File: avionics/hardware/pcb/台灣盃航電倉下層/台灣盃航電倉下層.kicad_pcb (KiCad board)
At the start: 4 copper layers, 80 x 80 mm, 43 parts, among them J1 XT60, J2 XT60, J4 Pyro1, J5 Pyro2, Q1 NMOS, Q2 NMOS, U3 LM2596S-5, U4 LM2596S-5, U5 AMS1117-3.3, U6 AMS1117-3.3

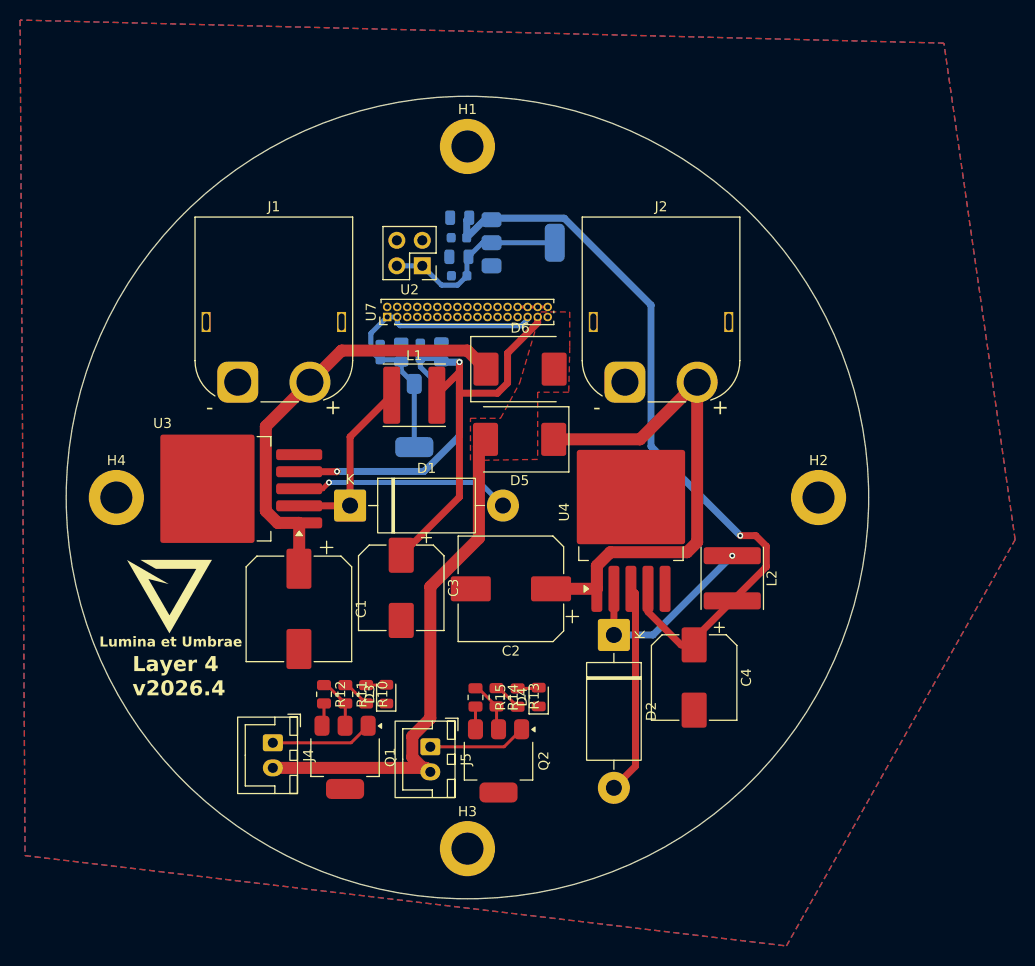
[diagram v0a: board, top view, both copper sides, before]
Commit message: Add files via upload
This is V1.1
add via stitch to increase heat dissipation capacity
change layer from 4 to 2, and increase thickness to 0.07mm
resolve the DRC problem
change the pad connection of the connector
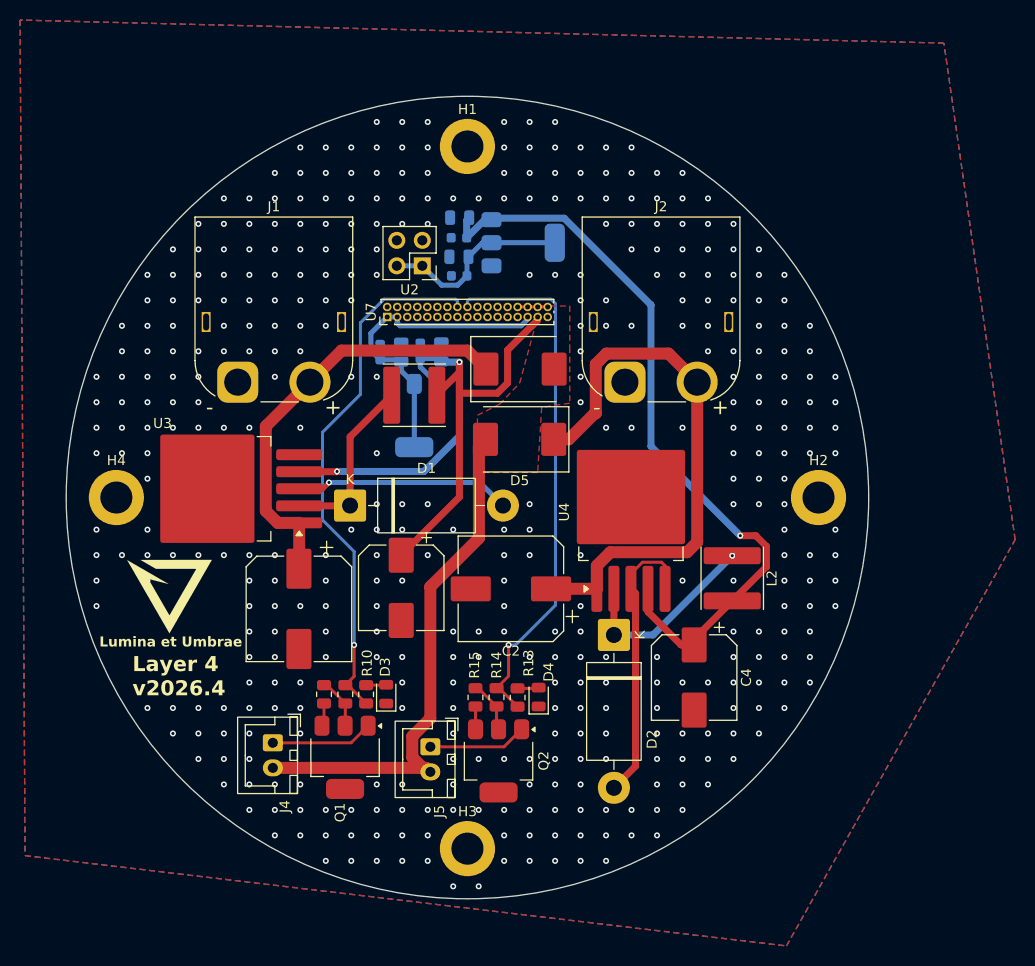
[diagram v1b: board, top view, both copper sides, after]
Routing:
- net PYRO2: track 2.87 -> 53.7 mm, vias 0 -> 1
- net PYRO1: track 2.83 -> 53.5 mm, vias 0 -> 1
- net GND: track 50.0 -> 57.8 mm, vias 1 -> 407
- net +BATT_b: track 50.4 -> 55.7 mm
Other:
- copper layers 4 -> 2

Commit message: V1.2
change Schottky Diode to nmos
change the footprint of the 1n5824*2
change the circuit of the LM2596S-5*2
change the position of the igition*2
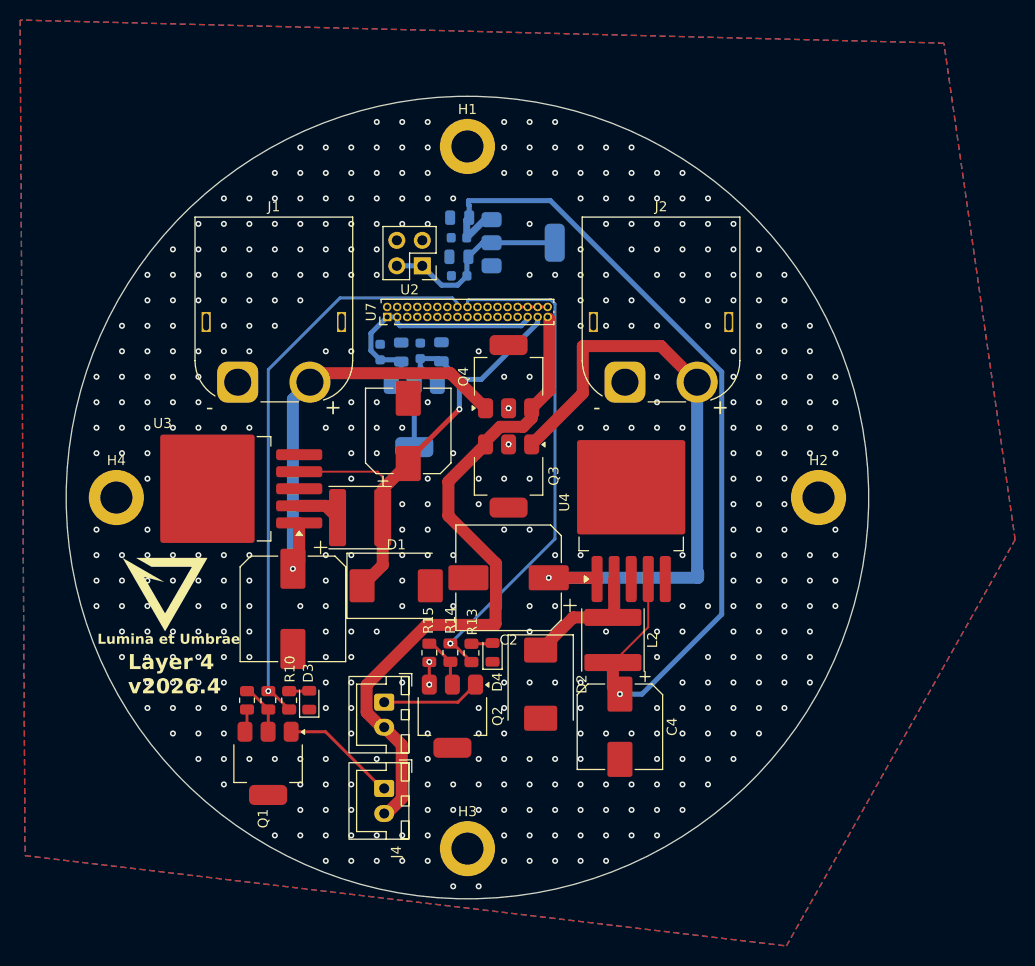
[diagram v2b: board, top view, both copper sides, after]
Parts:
- removed D5, D6: D_Schottky, Diode_SMD:D_SMC
- added Q3: NMOS, Package_TO_SOT_SMD:SOT-223, F.Cu at (151.1, 93.8)
- added Q4: NMOS, Package_TO_SOT_SMD:SOT-223, F.Cu at (151.1, 84.0)
- D1, D2: footprint Diode_THT:D_DO-201AD_P15.24mm_Horizontal -> Diode_SMD:D_SMC
- moved C3 15.7 mm to (141.1, 89.4), turned to 90 degrees
- moved L2 13.4 mm to (161.5, 110.2)
- moved L1 13.3 mm to (136.3, 98.0)
- moved J4 12.0 mm to (138.7, 125.0)
- moved D1 9.23 mm to (139.9, 104.8)
- moved C4 8.88 mm to (162.2, 118.8)
- moved D2 8.79 mm to (154.3, 114.6)
- moved D3 7.70 mm to (131.2, 116.2)
- moved Q1 7.70 mm to (127.1, 122.5)
- moved R10 7.70 mm to (129.2, 116.2)
- moved R11 7.70 mm to (127.2, 116.2)
- moved R12 7.70 mm to (125.0, 116.2)
- moved R15 6.40 mm to (143.2, 111.5)
- moved J5 6.40 mm to (138.7, 116.4)
- moved D4 6.40 mm to (149.5, 111.4)
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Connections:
- D1 pad 1: Net-(D1-K) -> +5V_m
- L1 pad 1: Net-(D1-K) -> Net-(U3-OUT)
- U3 pad 2: Net-(D1-K) -> Net-(U3-OUT)
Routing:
- net GND: track 57.8 -> 7.57 mm, vias 407 -> 437
- net Net-(D1-K): track 17.8 -> 0.00 mm
- net +BATT: track 53.0 -> 68.3 mm
- net +5V_b: track 75.7 -> 90.2 mm
- net +5V_m: track 70.0 -> 55.9 mm, vias 2 -> 1
- net +BATT_b: track 55.7 -> 64.1 mm, vias 0 -> 1
- net Net-(D2-K): track 19.7 -> 12.4 mm, vias 1 -> 0
- net Net-(U3-OUT): track 0.00 -> 4.31 mm
- net PYRO1: track 53.5 -> 57.3 mm
- net PYRO2: track 53.7 -> 50.6 mm
- net Net-(J4-Pin_1): track 10.2 -> 11.4 mm
- net +BATT_m: track 44.5 -> 43.5 mm, vias 0 -> 1
- removed copper zone on F.Cu, net +BATT

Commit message: 完成所有航電板設計
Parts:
- U2: footprint Connector_PinHeader_2.54mm:PinHeader_2x02_P2.54mm_Vertical -> Connector_PinHeader_1.00mm:PinHeader_2x02_P1.00mm_Vertical
- moved U2 1.50 mm to (141.0, 72.9)
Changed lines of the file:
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@@
 		)
 	)
-	(footprint "Connector_PinHeader_2.54mm:PinHeader_2x02_P2.54mm_Vertical"
+	(footprint "Connector_PinHeader_1.00mm:PinHeader_2x02_P1.00mm_Vertical"
 		(layer "F.Cu")
-		(at 142.5 72.9 180)
-		(descr "Through hole straight pin header, 2x02, 2.54mm pitch, double rows")
-		(tags "Through hole pin header THT 2x02 2.54mm double row")
+		(at 141 72.9 180)
+		(descr "Through hole straight pin header, 2x02, 1.00mm pitch, double rows")
+		(tags "Through hole pin header THT 2x02 1.00mm double row")
 		(property "Reference" "U2"
-			(at 1.27 -2.38 0)
+			(at 0.5 -1.61 180)
 			(layer "F.SilkS")
 			(effects
@@
 		)
 		(property "Value" "~"
-			(at 1.27 4.92 0)
+			(at 0.5 2.61 180)
 			(layer "F.Fab")
 			(effects
@@
 		)
 		(property "Datasheet" ""
-			(at 0 0 0)
+			(at 0 0 180)
 			(layer "F.Fab")
 			(hide yes)
@@
 		)
 		(property "Description" ""
-			(at 0 0 0)
+			(at 0 0 180)
 			(layer "F.Fab")
 			(hide yes)
@@
 		(sheetname "/")
 		(sheetfile "台灣盃航電倉下層.kicad_sch")
-		(zone_connect 2)
 		(attr through_hole)
 		(fp_line
-			(start 3.92 -1.38)
-			(end 3.92 3.92)
-			(stroke
-				(width 0.12)
-				(type solid)
-			)
-			(layer "F.SilkS")
-		)
-		(fp_line
-			(start 1.27 1.27)
-			(end 1.27 -1.38)
-			(stroke
-				(width 0.12)
-				(type solid)
-			)
-			(layer "F.SilkS")
-		)
-		(fp_line
-			(start 1.27 -1.38)
-			(end 3.92 -1.38)
-			(stroke
-				(width 0.12)
-				(type solid)
-			)
-			(layer "F.SilkS")
-		)
-		(fp_line
-			(start -1.38 3.92)
-			(end 3.92 3.92)
-			(stroke
-				(width 0.12)
-				(type solid)
-			)
-			(layer "F.SilkS")
-		)
-		(fp_line
-			(start -1.38 1.27)
-			(end 1.27 1.27)
-			(stroke
-				(width 0.12)
-				(type solid)
-			)
-			(layer "F.SilkS")
-		)
-		(fp_line
-			(start -1.38 1.27)
-			(end -1.38 3.92)
-			(stroke
-				(width 0.12)
-				(type solid)
-			)
-			(layer "F.SilkS")
-		)
-		(fp_line
-			(start -1.38 0)
-			(end -1.38 -1.38)
-			(stroke
-				(width 0.12)
-				(type solid)
-			)
-			(layer "F.SilkS")
-		)
-		(fp_line
-			(start -1.38 -1.38)
-			(end 0 -1.38)
+			(start 1.76 -0.61)
+			(end 1.76 1.61)
+			(stroke
+				(width 0.12)
+				(type solid)
+			)
+			(layer "F.SilkS")
+		)
+		(fp_line
+			(start 1.41003 1.61)
+			(end 1.76 1.61)
+			(stroke
+				(width 0.12)
+				(type solid)
+			)
+			(layer "F.SilkS")
+		)
+		(fp_line
+			(start 1.41003 -0.61)
+			(end 1.76 -0.61)
+			(stroke
+				(width 0.12)
+				(type solid)
+			)
+			(layer "F.SilkS")
+		)
+		(fp_line
+			(start 0.41003 1.61)
+			(end 0.58997 1.61)
+			(stroke
+				(width 0.12)
+				(type solid)
+			)
+			(layer "F.SilkS")
+		)
+		(fp_line
+			(start -0.76 1.61)
+			(end -0.41003 1.61)
+			(stroke
+				(width 0.12)
+				(type solid)
+			)
+			(layer "F.SilkS")
+		)
+		(fp_line
+			(start -0.76 0.735)
+			(end -0.685565 0.735)
+			(stroke
+				(width 0.12)
+				(type solid)
+			)
+			(layer "F.SilkS")
+		)
+		(fp_line
+			(start -0.76 0.735)
+			(end -0.76 1.61)
+			(stroke
+				(width 0.12)
+				(type solid)
+			)
+			(layer "F.SilkS")
+		)
+		(fp_line
+			(start -0.76 0)
+			(end -0.76 -0.735)
+			(stroke
+				(width 0.12)
+				(type solid)
+			)
+			(layer "F.SilkS")
+		)
+		(fp_line
+			(start -0.76 -0.735)
+			(end 0 -0.735)
 			(stroke
 				(width 0.12)
@@
 		)
 		(fp_rect
-			(start -1.77 -1.77)
-			(end 4.32 4.32)
+			(start -1.15 -1)
+			(end 2.15 2)
 			(stroke
 				(width 0.05)
@@
 		)
 		(fp_line
-			(start 3.81 3.81)
-			(end -1.27 3.81)
-			(stroke
-				(width 0.1)
-				(type solid)
-			)
-			(layer "F.Fab")
-		)
-		(fp_line
-			(start 3.81 -1.27)
-			(end 3.81 3.81)
-			(stroke
-				(width 0.1)
-				(type solid)
-			)
-			(layer "F.Fab")
-		)
-		(fp_line
-			(start 0 -1.27)
-			(end 3.81 -1.27)
-			(stroke
-				(width 0.1)
-				(type solid)
-			)
-			(layer "F.Fab")
-		)
-		(fp_line
-			(start -1.27 3.81)
-			(end -1.27 0)
-			(stroke
-				(width 0.1)
-				(type solid)
-			)
-			(layer "F.Fab")
-		)
-		(fp_line
-			(start -1.27 0)
-			(end 0 -1.27)
+			(start 1.65 1.5)
+			(end -0.65 1.5)
+			(stroke
+				(width 0.1)
+				(type solid)
+			)
+			(layer "F.Fab")
+		)
+		(fp_line
+			(start 1.65 -0.5)
+			(end 1.65 1.5)
+			(stroke
+				(width 0.1)
+				(type solid)
+			)
+			(layer "F.Fab")
+		)
+		(fp_line
+			(start -0.075 -0.5)
+			(end 1.65 -0.5)
+			(stroke
+				(width 0.1)
+				(type solid)
+			)
+			(layer "F.Fab")
+		)
+		(fp_line
+			(start -0.65 1.5)
+			(end -0.65 0.075)
+			(stroke
+				(width 0.1)
+				(type solid)
+			)
+			(layer "F.Fab")
+		)
+		(fp_line
+			(start -0.65 0.075)
+			(end -0.075 -0.5)
 			(stroke
 				(width 0.1)
@@
 		)
 		(fp_text user "${REFERENCE}"
-			(at 1.27 1.27 90)
+			(at 0.5 0.5 270)
 			(layer "F.Fab")
 			(effects
@@
 		(pad "1" thru_hole rect
 			(at 0 0 180)
-			(size 1.7 1.7)
-			(drill 1)
+			(size 0.85 0.85)
+			(drill 0.5)
 			(layers "*.Cu" "*.Mask")
 			(remove_unused_layers no)
@@
 		)
 		(pad "2" thru_hole circle
-			(at 2.54 0 180)
-			(size 1.7 1.7)
-			(drill 1)
+			(at 1 0 180)
+			(size 0.85 0.85)
+			(drill 0.5)
 			(layers "*.Cu" "*.Mask")
 			(remove_unused_layers no)
@@
 		)
 		(pad "3" thru_hole circle
-			(at 0 2.54 180)
-			(size 1.7 1.7)
-			(drill 1)
+			(at 0 1 180)
+			(size 0.85 0.85)
+			(drill 0.5)
 			(layers "*.Cu" "*.Mask")
 			(remove_unused_layers no)
@@
 		)
 		(pad "4" thru_hole circle
-			(at 2.54 2.54 180)
-			(size 1.7 1.7)
-			(drill 1)
+			(at 1 1 180)
+			(size 0.85 0.85)
+			(drill 0.5)
 			(layers "*.Cu" "*.Mask")
 			(remove_unused_layers no)
@@
 		)
 		(embedded_fonts no)
-		(model "${KICAD9_3DMODEL_DIR}/Connector_PinHeader_2.54mm.3dshapes/PinHeader_2x02_P2.54mm_Vertical.step"
+		(model "${KICAD9_3DMODEL_DIR}/Connector_PinHeader_1.00mm.3dshapes/PinHeader_2x02_P1.00mm_Vertical.step"
 			(offset
 				(xyz 0 0 0)
